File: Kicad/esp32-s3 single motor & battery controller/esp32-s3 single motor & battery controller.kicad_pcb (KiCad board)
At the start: 4 copper layers, 44.9 x 42 mm, 133 parts, among them J1 JST SH SM04B, J2 7 pin FPC 0.3mm, J3 Conn_01x03, J4 Conn_01x03, J5 Batt Balance connector, Q1 NMOS,12v, Q2 NMOS, 12v, Q3 NMOS,12v,PPak, Q4 NMOS, 12v, Q5 NMOS, 12v, Q7 NMOS,12v,PPak, SW1 SW_Push, SW2 SW_Push, U2 AP63203WU, U3 BQ76905RGRR, U4 BQ24780SRUYR, U5 ESP32-S3, U6 74HC595, Y1 40mhz, 10ppm

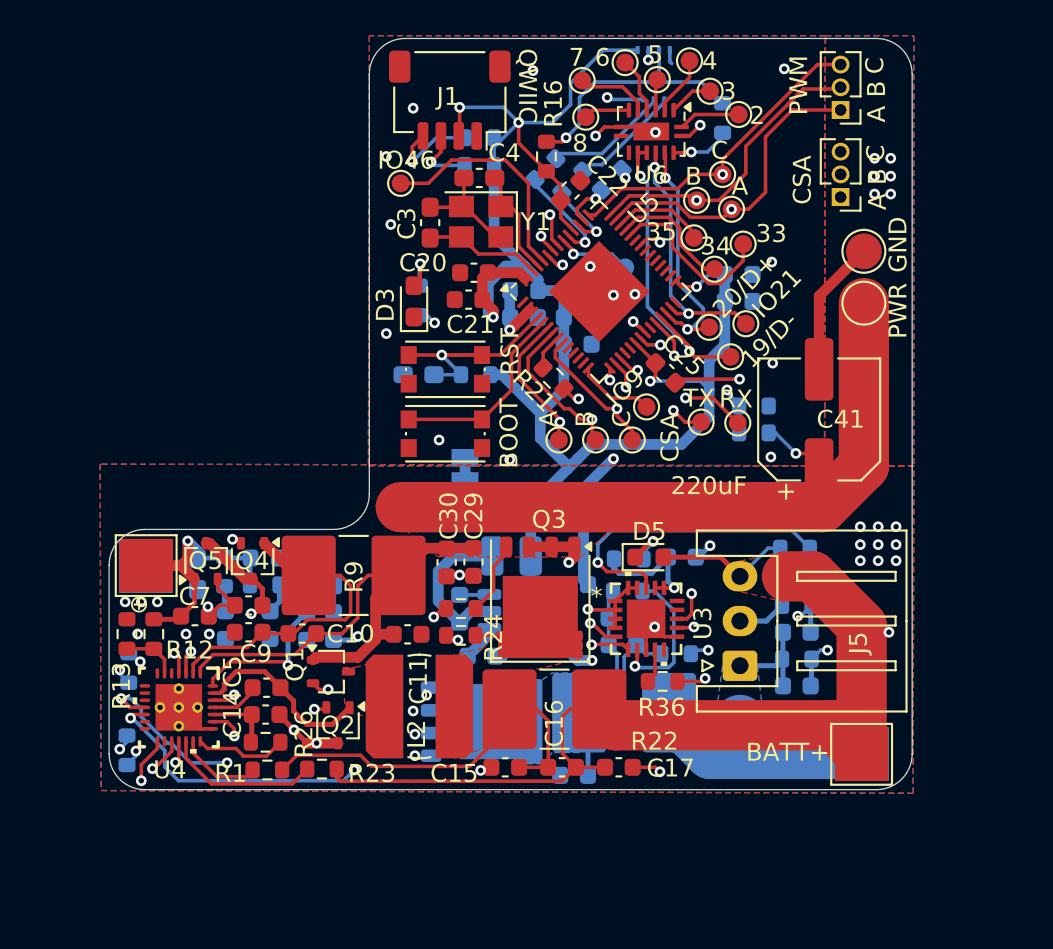
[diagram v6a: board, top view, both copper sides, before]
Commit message: Making a few changes to layout based on spotted problems
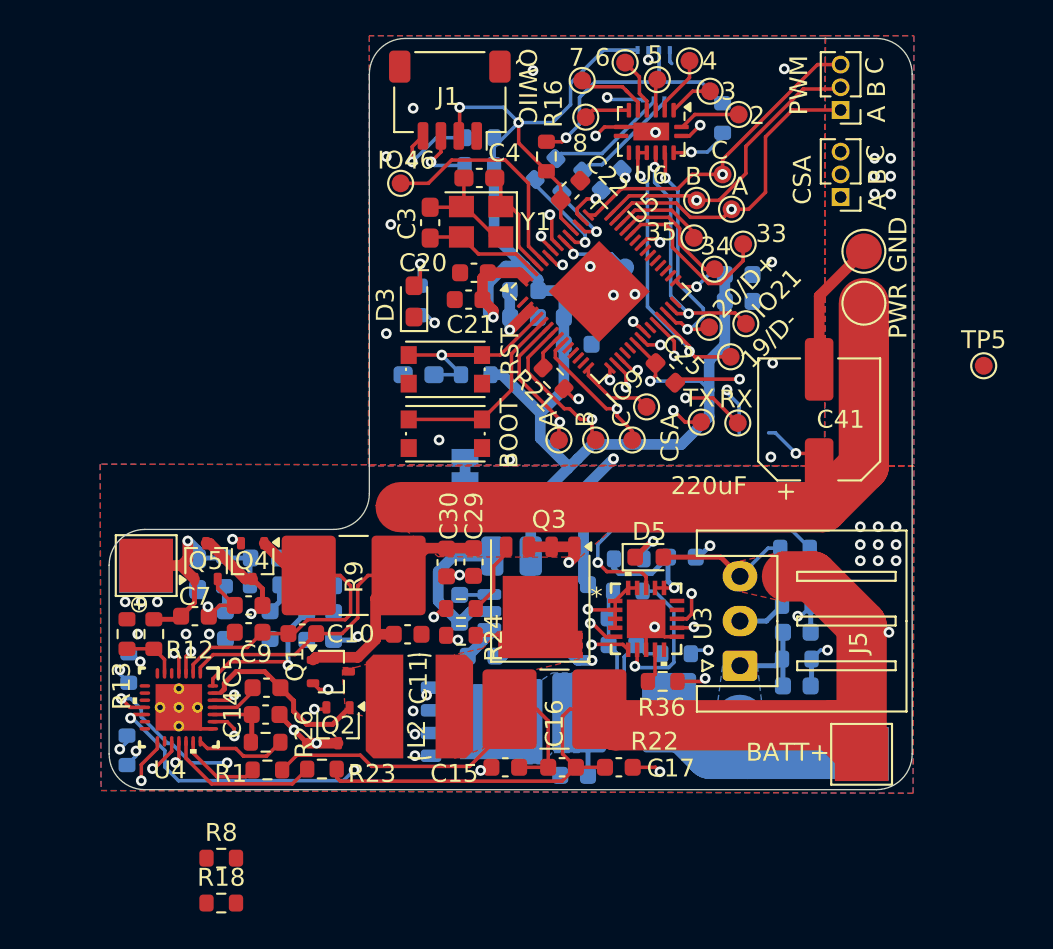
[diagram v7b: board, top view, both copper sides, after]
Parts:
- removed R17: 100k, Resistor_SMD:R_0603_1608Metric
- added R8: 10k, Resistor_SMD:R_0603_1608Metric, F.Cu at (114.4, 135.8)
- added TP5: ~, TestPoint:TestPoint_Pad_D1.0mm, F.Cu at (157.0, 108.3)
- C41: value 220uF -> 220uF,APA0609221M016R
- R18: value 150k -> 10k; moved to F.Cu
- R26: value 100k -> 10k
- SW1, SW2: value SW_Push -> KMR2
- moved R18 40.7 mm to (114.4, 138.3), turned to 0 degrees
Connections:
- C37 pad 2: /PSU/BATT- -> Net-(J5-Pin_1)
- C39 pad 2: /PSU/BATT- -> Net-(J5-Pin_1)
- J5 pad 1: /PSU/BATT- -> Net-(J5-Pin_1)
- R18 pad 1: GND -> /PSU/REGN
- R18 pad 2: /VBATT -> Net-(U4-TB_STAT_N)
- R35 pad 2: /PSU/BATT- -> Net-(J5-Pin_1)
- U4 pad 13: unconnected-(U4-CMPIN-Pad13) -> GNDPWR
- U4 pad 16: unconnected-(U4-TB_STAT_N-Pad16) -> Net-(U4-TB_STAT_N)
- U4 pad 5: unconnected-(U4-ACOK-Pad5) -> Net-(U4-ACOK)
- U5 pad 24: /VBATT -> Net-(U5-GPIO18)
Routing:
- net Net-(U5-GPIO18): track 0.00 -> 8.80 mm, vias 0 -> 2
- net /VBATT: track 8.80 -> 0.00 mm, vias 2 -> 0
- net Net-(J5-Pin_1): track 0.00 -> 5.51 mm
- net /PSU/BATT-: track 28.8 -> 23.3 mm

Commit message: Replacing sense resistors, started routing additional pullup resistors
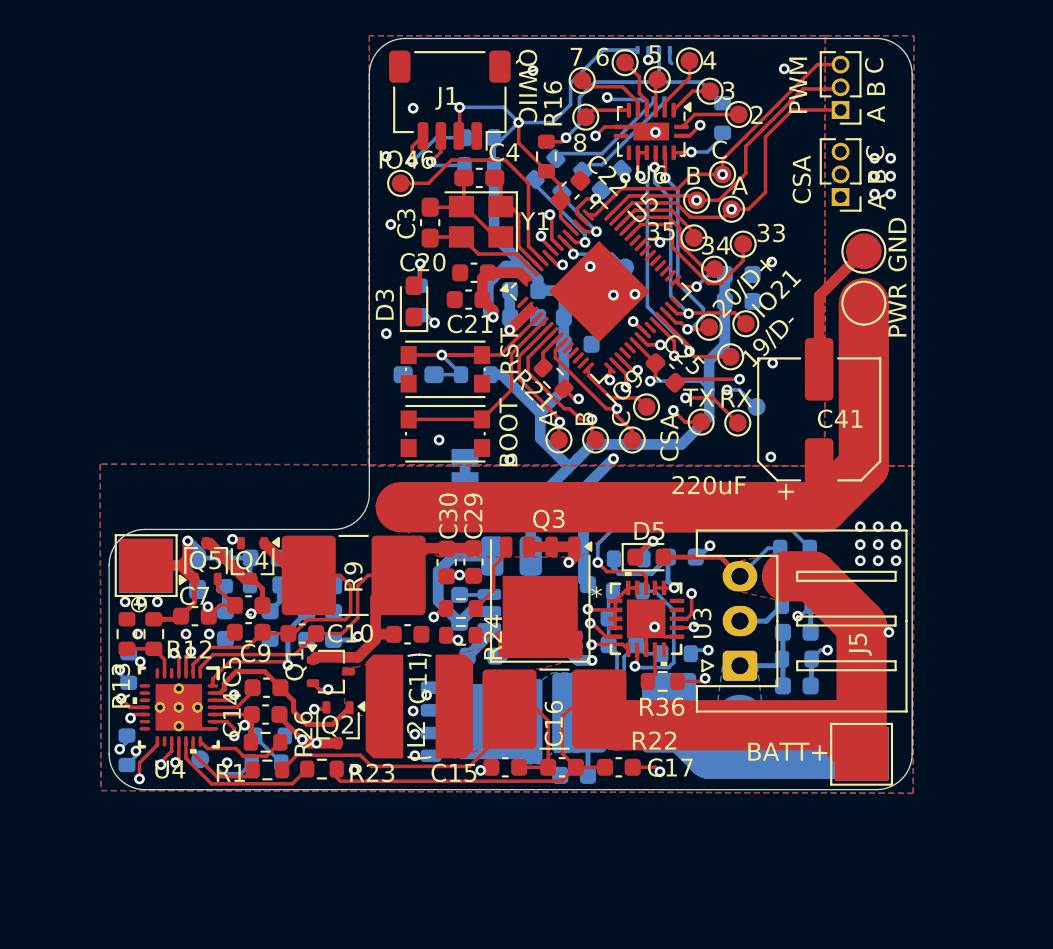
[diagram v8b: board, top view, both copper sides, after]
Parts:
- added TP6: ~, TestPoint:TestPoint_Pad_D1.0mm, B.Cu at (113.2, 130.3)
- R18, R8, TP5: moved to B.Cu
- R22: value 10mOhm, CS -> 5mOhm, CS
- R27: value 10mOhm, CS -> 1mOhm, CS
- R9: value 10mOhm CS -> 5mOhm CS
- moved TP5 12.9 mm to (144.3, 110.6), turned to 180 degrees
- moved R18 8.24 mm to (116.9, 130.5), turned to 180 degrees
- moved R8 7.36 mm to (117.1, 129.0)
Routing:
- net /MOTORPWR: track 85.7 -> 81.5 mm, vias 3 -> 2
- net /PSU/REGN: track 3.75 -> 7.79 mm, vias 0 -> 1
- net Net-(U4-TB_STAT_N): track 0.00 -> 2.21 mm
- net Net-(U4-BATSRC): track 23.1 -> 22.2 mm
- net Net-(U5-GPIO18): track 8.80 -> 8.23 mm
